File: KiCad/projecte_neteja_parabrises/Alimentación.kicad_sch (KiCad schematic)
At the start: 12 parts, among them U1 LM1117DT-3.3, U2 LM2596S-5

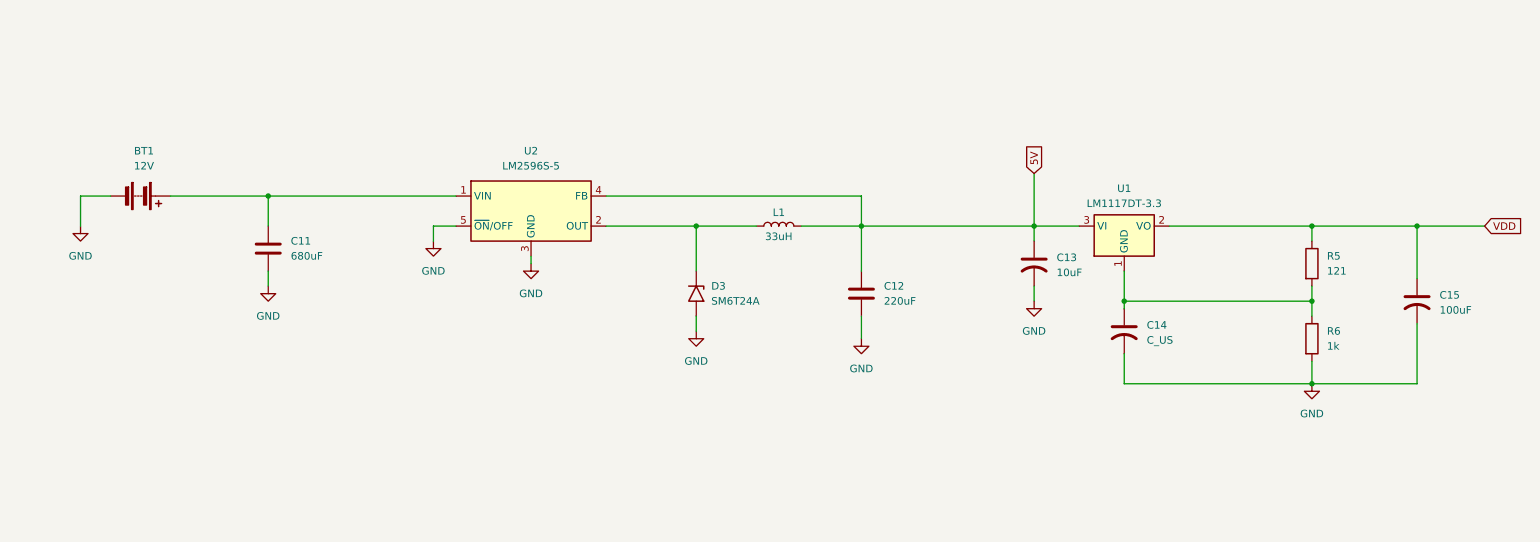
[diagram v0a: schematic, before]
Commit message: millora alimentacio
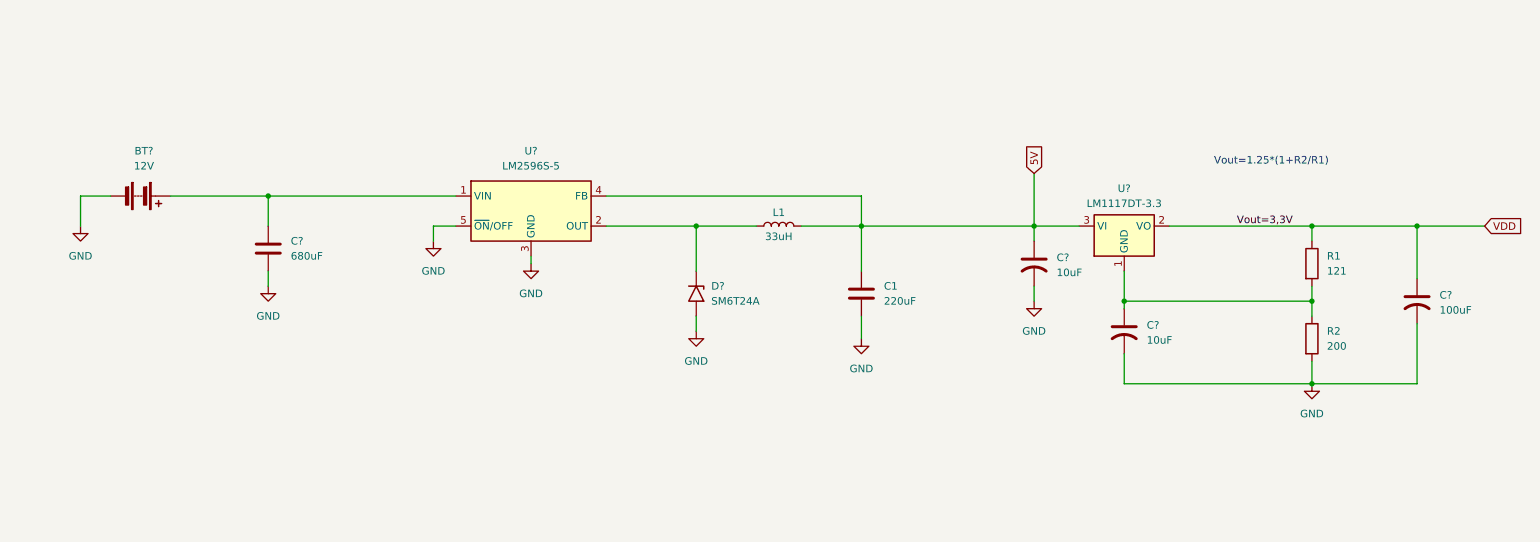
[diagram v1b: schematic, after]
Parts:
- C?: renamed from C14; value C_US -> 10uF
- R2: renamed from R6; value 1k -> 200
- renumbered BT1 to BT?, C12 to C1, C13 to C?, C11 to C?, C15 to C?, D3 to D?, R5 to R1, U1 to U?, U2 to U?
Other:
- note added: "Vout=1.25*(1+R2/R1)"
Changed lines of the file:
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@@
 	(generator_version "9.0")
 	(paper "A4")
+	(text "Vout=1.25*(1+R2/R1)"
+		(exclude_from_sim no)
+		(at 229.362 74.168 0)
+		(effects
+			(font
+				(size 1.27 1.27)
+			)
+		)
+	)
 	(junction
 		(at 254 85.09)
@@
 		)
 	)
+	(label "Vout=3,3V"
+		(at 223.52 85.09 0)
+		(effects
+			(font
+				(size 1.27 1.27)
+			)
+			(justify left bottom)
+		)
+	)
 	(global_label "VDD"
 		(shape input)
@@
 		(dnp no)
 		(fields_autoplaced yes)
-		(property "Reference" "#PWR018"
+		(property "Reference" "#PWR?"
 			(at 236.22 118.11 0)
 			(effects
@@
 		(dnp no)
 		(fields_autoplaced yes)
-		(property "Reference" "U1"
+		(property "Reference" "U?"
 			(at 204.47 78.74 0)
 			(effects
@@
 		(dnp no)
 		(fields_autoplaced yes)
-		(property "Reference" "R6"
+		(property "Reference" "R2"
 			(at 238.76 102.8699 0)
 			(effects
@@
 			)
 		)
-		(property "Value" "1k"
+		(property "Value" "200"
 			(at 238.76 105.4099 0)
 			(effects
@@
 			(project "Alimentación"
 				(path "/2ad4f79a-6f2e-459e-be48-40e5d52d2cdd"
-					(reference "R?")
+					(reference "R2")
 					(unit 1)
 				)
@@
 		(dnp no)
 		(fields_autoplaced yes)
-		(property "Reference" "C13"
+		(property "Reference" "C?"
 			(at 193.04 90.4239 0)
 			(effects
@@
 		(dnp no)
 		(fields_autoplaced yes)
-		(property "Reference" "#PWR0105"
+		(property "Reference" "#PWR02"
 			(at 160.02 110.49 0)
 			(effects
@@
 		(dnp no)
 		(fields_autoplaced yes)
-		(property "Reference" "#PWR0104"
+		(property "Reference" "#PWR01"
 			(at 87.63 93.98 0)
 			(effects
@@
 		(dnp no)
 		(fields_autoplaced yes)
-		(property "Reference" "#PWR017"
+		(property "Reference" "#PWR?"
 			(at 189.23 104.14 0)
 			(effects
@@
 		(dnp no)
 		(fields_autoplaced yes)
-		(property "Reference" "#PWR015"
+		(property "Reference" "#PWR?"
 			(at 59.69 101.6 0)
 			(effects
@@
 		(dnp no)
 		(fields_autoplaced yes)
-		(property "Reference" "#PWR014"
+		(property "Reference" "#PWR?"
 			(at 132.08 109.22 0)
 			(effects
@@
 		(dnp no)
 		(fields_autoplaced yes)
-		(property "Reference" "C12"
+		(property "Reference" "C1"
 			(at 163.83 95.2499 0)
 			(effects
@@
 		(dnp no)
 		(fields_autoplaced yes)
-		(property "Reference" "BT1"
+		(property "Reference" "BT?"
 			(at 38.6715 72.39 90)
 			(effects
@@
 		(dnp no)
 		(fields_autoplaced yes)
-		(property "Reference" "C11"
+		(property "Reference" "C?"
 			(at 63.5 87.6299 0)
 			(effects
@@
 		(dnp no)
 		(fields_autoplaced yes)
-		(property "Reference" "R5"
+		(property "Reference" "R1"
 			(at 238.76 90.1699 0)
 			(effects
@@
 			(project "Alimentación"
 				(path "/2ad4f79a-6f2e-459e-be48-40e5d52d2cdd"
-					(reference "R?")
+					(reference "R1")
 					(unit 1)
 				)
@@
 		(dnp no)
 		(fields_autoplaced yes)
-		(property "Reference" "U2"
+		(property "Reference" "U?"
 			(at 104.14 72.39 0)
 			(effects
@@
 		(dnp no)
 		(fields_autoplaced yes)
-		(property "Reference" "#PWR02"
+		(property "Reference" "#PWR?"
 			(at 104.14 97.79 0)
 			(effects
@@
 		(dnp no)
 		(fields_autoplaced yes)
-		(property "Reference" "#PWR01"
+		(property "Reference" "#PWR?"
 			(at 27.94 91.44 0)
 			(effects
@@
 		(dnp no)
 		(fields_autoplaced yes)
-		(property "Reference" "C15"
+		(property "Reference" "C?"
 			(at 257.81 96.7739 0)
 			(effects
@@
 		(dnp no)
 		(fields_autoplaced yes)
-		(property "Reference" "D3"
+		(property "Reference" "D?"
 			(at 134.62 95.2499 90)
 			(effects
@@
 		(dnp no)
 		(fields_autoplaced yes)
-		(property "Reference" "C14"
+		(property "Reference" "C?"
 			(at 208.28 101.8539 0)
 			(effects
@@
 			)
 		)
-		(property "Value" "C_US"
+		(property "Value" "10uF"
 			(at 208.28 104.3939 0)
 			(effects

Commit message: Actualización huellas
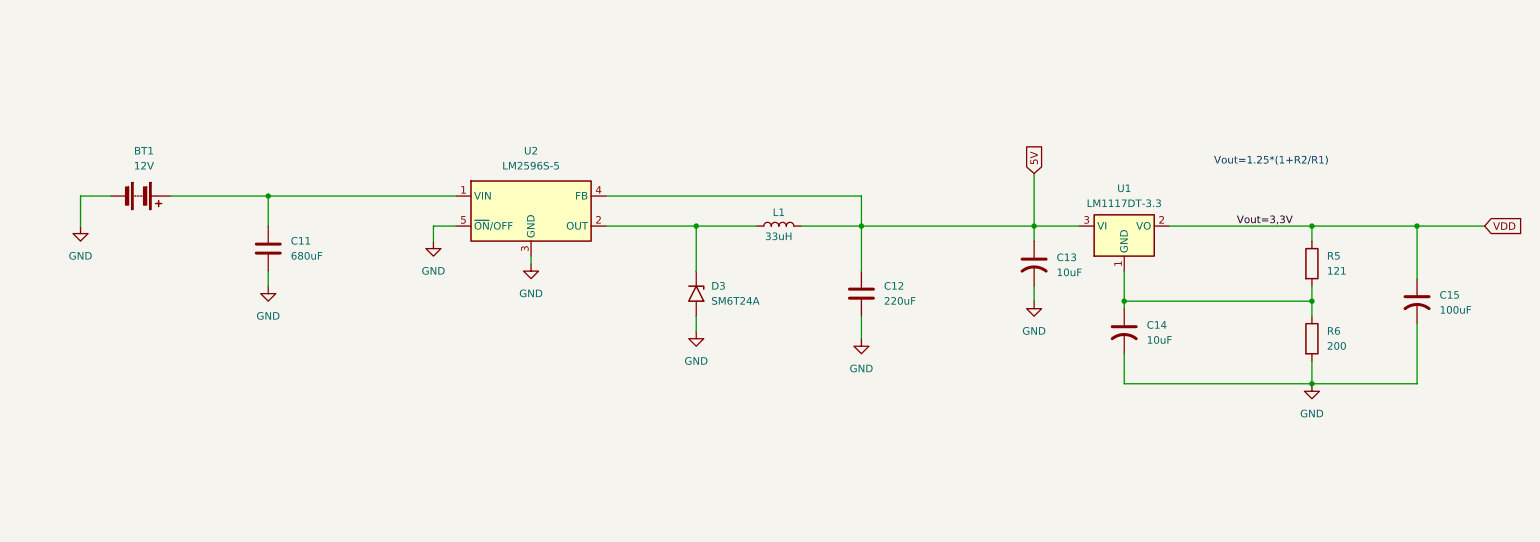
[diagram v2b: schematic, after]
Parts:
- L1: footprint (none) -> Inductor_SMD:L_0603_1608Metric_Pad1.05x0.95mm_HandSolder
- gave numbers to parts that had none: 8
- renumbered C1 to C12, R1 to R5, R2 to R6
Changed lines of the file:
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@@
 		(dnp no)
 		(fields_autoplaced yes)
-		(property "Reference" "#PWR?"
+		(property "Reference" "#PWR018"
 			(at 236.22 118.11 0)
 			(effects
@@
 		(dnp no)
 		(fields_autoplaced yes)
-		(property "Reference" "U?"
+		(property "Reference" "U1"
 			(at 204.47 78.74 0)
 			(effects
@@
 		(dnp no)
 		(fields_autoplaced yes)
-		(property "Reference" "R2"
+		(property "Reference" "R6"
 			(at 238.76 102.8699 0)
 			(effects
@@
 		(dnp no)
 		(fields_autoplaced yes)
-		(property "Reference" "C?"
+		(property "Reference" "C13"
 			(at 193.04 90.4239 0)
 			(effects
@@
 		(dnp no)
 		(fields_autoplaced yes)
-		(property "Reference" "#PWR02"
+		(property "Reference" "#PWR0105"
 			(at 160.02 110.49 0)
 			(effects
@@
 		(dnp no)
 		(fields_autoplaced yes)
-		(property "Reference" "#PWR01"
+		(property "Reference" "#PWR0104"
 			(at 87.63 93.98 0)
 			(effects
@@
 		(dnp no)
 		(fields_autoplaced yes)
-		(property "Reference" "#PWR?"
+		(property "Reference" "#PWR017"
 			(at 189.23 104.14 0)
 			(effects
@@
 		(dnp no)
 		(fields_autoplaced yes)
-		(property "Reference" "#PWR?"
+		(property "Reference" "#PWR015"
 			(at 59.69 101.6 0)
 			(effects
@@
 		(dnp no)
 		(fields_autoplaced yes)
-		(property "Reference" "#PWR?"
+		(property "Reference" "#PWR014"
 			(at 132.08 109.22 0)
 			(effects
@@
 		(dnp no)
 		(fields_autoplaced yes)
-		(property "Reference" "C1"
+		(property "Reference" "C12"
 			(at 163.83 95.2499 0)
 			(effects
@@
 		(dnp no)
 		(fields_autoplaced yes)
-		(property "Reference" "BT?"
+		(property "Reference" "BT1"
 			(at 38.6715 72.39 90)
 			(effects
@@
 		(dnp no)
 		(fields_autoplaced yes)
-		(property "Reference" "C?"
+		(property "Reference" "C11"
 			(at 63.5 87.6299 0)
 			(effects
@@
 		(dnp no)
 		(fields_autoplaced yes)
-		(property "Reference" "R1"
+		(property "Reference" "R5"
 			(at 238.76 90.1699 0)
 			(effects
@@
 		(dnp no)
 		(fields_autoplaced yes)
-		(property "Reference" "U?"
+		(property "Reference" "U2"
 			(at 104.14 72.39 0)
 			(effects
@@
 		(dnp no)
 		(fields_autoplaced yes)
-		(property "Reference" "#PWR?"
+		(property "Reference" "#PWR02"
 			(at 104.14 97.79 0)
 			(effects
@@
 		(dnp no)
 		(fields_autoplaced yes)
-		(property "Reference" "#PWR?"
+		(property "Reference" "#PWR01"
 			(at 27.94 91.44 0)
 			(effects
@@
 		(dnp no)
 		(fields_autoplaced yes)
-		(property "Reference" "C?"
+		(property "Reference" "C15"
 			(at 257.81 96.7739 0)
 			(effects
@@
 			)
 		)
-		(property "Footprint" ""
+		(property "Footprint" "Inductor_SMD:L_0603_1608Metric_Pad1.05x0.95mm_HandSolder"
 			(at 146.05 85.09 0)
 			(effects
@@
 		(dnp no)
 		(fields_autoplaced yes)
-		(property "Reference" "D?"
+		(property "Reference" "D3"
 			(at 134.62 95.2499 90)
 			(effects
@@
 		(dnp no)
 		(fields_autoplaced yes)
-		(property "Reference" "C?"
+		(property "Reference" "C14"
 			(at 208.28 101.8539 0)
 			(effects

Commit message: huella bateria
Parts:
- BT1: footprint (none) -> TerminalBlock:TerminalBlock_MaiXu_MX126-5.0-02P_1x02_P5.00mm
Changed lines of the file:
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@@
 			)
 		)
-		(property "Footprint" ""
+		(property "Footprint" "TerminalBlock:TerminalBlock_MaiXu_MX126-5.0-02P_1x02_P5.00mm"
 			(at 39.624 80.01 90)
 			(effects

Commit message: huella c electrolitica
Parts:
- C13, C14, C15: footprint Capacitor_SMD:C_0805_2012Metric -> Capacitor_THT:CP_Radial_D5.0mm_P2.50mm
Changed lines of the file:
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@@
 			)
 		)
-		(property "Footprint" "Capacitor_SMD:C_0805_2012Metric"
+		(property "Footprint" "Capacitor_THT:CP_Radial_D5.0mm_P2.50mm"
 			(at 189.23 91.44 0)
 			(effects
@@
 			)
 		)
-		(property "Footprint" "Capacitor_SMD:C_0805_2012Metric"
+		(property "Footprint" "Capacitor_THT:CP_Radial_D5.0mm_P2.50mm"
 			(at 254 97.79 0)
 			(effects
@@
 			)
 		)
-		(property "Footprint" "Capacitor_SMD:C_0805_2012Metric"
+		(property "Footprint" "Capacitor_THT:CP_Radial_D5.0mm_P2.50mm"
 			(at 204.47 102.87 0)
 			(effects

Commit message: formula
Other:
- note added: "Vout=1.25*(1+R5/R6)"
- note removed: "Vout=1.25*(1+R2/R1)"
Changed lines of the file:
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@@
 	(generator_version "9.0")
 	(paper "A4")
-	(text "Vout=1.25*(1+R2/R1)"
+	(text "Vout=1.25*(1+R5/R6)"
 		(exclude_from_sim no)
 		(at 229.362 74.168 0)

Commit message: Led
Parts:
- added D2: LED, LED_SMD:LED_0805_2012Metric_Pad1.15x1.40mm_HandSolder, symbol Device:LED
- added R8: 1k, Resistor_SMD:R_0603_1608Metric_Pad0.98x0.95mm_HandSolder, symbol Device:R
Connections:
- net GND: now also R8.1
- new net: D2.1 (K), R8.2
- new net VCC: D2.2 (A)

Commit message: potencia cambios
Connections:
- net VCC is gone; now on net VDD: D2.2 (A)
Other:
- moved on the sheet: D2, R8
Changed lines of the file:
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@@
 	(wire
 		(pts
-			(xy 40.005 128.27) (xy 40.005 130.175)
+			(xy 229.235 55.88) (xy 229.235 57.785)
 		)
 		(stroke
@@
 	(wire
 		(pts
+			(xy 245.11 55.88) (xy 254 55.88)
+		)
+		(stroke
+			(width 0)
+			(type default)
+		)
+	)
+	(wire
+		(pts
 			(xy 236.22 111.76) (xy 254 111.76)
 		)
@@
 	(wire
 		(pts
-			(xy 40.64 128.27) (xy 40.005 128.27)
+			(xy 229.87 55.88) (xy 229.235 55.88)
 		)
 		(stroke
@@
 		(pts
 			(xy 204.47 106.68) (xy 204.47 111.76)
+		)
+		(stroke
+			(width 0)
+			(type default)
+		)
+	)
+	(wire
+		(pts
+			(xy 254 55.88) (xy 254 85.09)
 		)
 		(stroke
@@
 			)
 			(justify left bottom)
-		)
-	)
-	(global_label "VCC"
-		(shape input)
-		(at 55.88 128.27 0)
-		(fields_autoplaced yes)
-		(effects
-			(font
-				(size 1.27 1.27)
-			)
-			(justify left)
-		)
-		(property "Intersheetrefs" "${INTERSHEET_REFS}"
-			(at 62.4938 128.27 0)
-			(effects
-				(font
-					(size 1.27 1.27)
-				)
-				(justify left)
-				(hide yes)
-			)
 		)
 	)
@@
 	(symbol
 		(lib_id "power:GND")
-		(at 40.005 130.175 0)
+		(at 229.235 57.785 0)
 		(unit 1)
 		(exclude_from_sim no)
@@
 		(fields_autoplaced yes)
 		(property "Reference" "#PWR038"
-			(at 40.005 136.525 0)
+			(at 229.235 64.135 0)
 			(effects
 				(font
@@
 		)
 		(property "Value" "GND"
-			(at 40.005 135.255 0)
+			(at 229.235 62.865 0)
 			(effects
 				(font
@@
 		)
 		(property "Footprint" ""
-			(at 40.005 130.175 0)
+			(at 229.235 57.785 0)
 			(effects
 				(font
@@
 		)
 		(property "Datasheet" ""
-			(at 40.005 130.175 0)
+			(at 229.235 57.785 0)
 			(effects
 				(font
@@
 		)
 		(property "Description" "Power symbol creates a global label with name \"GND\" , ground"
-			(at 40.005 130.175 0)
+			(at 229.235 57.785 0)
 			(effects
 				(font
@@
 		)
 		(instances
+			(project "Alimentación"
+				(path "/2ad4f79a-6f2e-459e-be48-40e5d52d2cdd"
+					(reference "#PWR?")
+					(unit 1)
+				)
+			)
 			(project "projecte_neteja_parabrises"
 				(path "/83fe8808-b70b-463e-9fcd-89556c9690a9/a8962c48-b3a9-4541-b459-e1566624b900"
@@
 	(symbol
 		(lib_id "Device:LED")
-		(at 52.07 128.27 0)
+		(at 241.3 55.88 0)
 		(unit 1)
 		(exclude_from_sim no)
@@
 		(fields_autoplaced yes)
 		(property "Reference" "D2"
-			(at 50.4825 122.555 0)
+			(at 239.7125 50.165 0)
 			(effects
 				(font
@@
 		)
 		(property "Value" "LED"
-			(at 50.4825 125.095 0)
+			(at 239.7125 52.705 0)
 			(effects
 				(font
@@
 		)
 		(property "Footprint" "LED_SMD:LED_0805_2012Metric_Pad1.15x1.40mm_HandSolder"
-			(at 52.07 128.27 0)
+			(at 241.3 55.88 0)
 			(effects
 				(font
@@
 		)
 		(property "Datasheet" "~"
-			(at 52.07 128.27 0)
+			(at 241.3 55.88 0)
 			(effects
 				(font
@@
 		)
 		(property "Description" "Light emitting diode"
-			(at 52.07 128.27 0)
+			(at 241.3 55.88 0)
 			(effects
 				(font
@@
 		)
 		(property "Sim.Pins" "1=K 2=A"
-			(at 52.07 128.27 0)
+			(at 241.3 55.88 0)
 			(effects
 				(font
@@
 		)
 		(instances
+			(project "Alimentación"
+				(path "/2ad4f79a-6f2e-459e-be48-40e5d52d2cdd"
+					(reference "D?")
+					(unit 1)
+				)
+			)
 			(project "projecte_neteja_parabrises"
 				(path "/83fe8808-b70b-463e-9fcd-89556c9690a9/a8962c48-b3a9-4541-b459-e1566624b900"
@@
 	(symbol
 		(lib_id "Device:R")
-		(at 44.45 128.27 90)
+		(at 233.68 55.88 90)
 		(unit 1)
 		(exclude_from_sim no)
@@
 		(fields_autoplaced yes)
 		(property "Reference" "R8"
-			(at 44.45 122.555 90)
+			(at 233.68 50.165 90)
 			(effects
 				(font
@@
 		)
 		(property "Value" "1k"
-			(at 44.45 125.095 90)
+			(at 233.68 52.705 90)
 			(effects
 				(font
@@
 		)
 		(property "Footprint" "Resistor_SMD:R_0603_1608Metric_Pad0.98x0.95mm_HandSolder"
-			(at 44.45 130.048 90)
+			(at 233.68 57.658 90)
 			(effects
 				(font
@@
 		)
 		(property "Datasheet" "~"
-			(at 44.45 128.27 0)
+			(at 233.68 55.88 0)
 			(effects
 				(font
@@
 		)
 		(property "Description" "Resistor"
-			(at 44.45 128.27 0)
+			(at 233.68 55.88 0)
 			(effects
 				(font
@@
 		)
 		(instances
+			(project "Alimentación"
+				(path "/2ad4f79a-6f2e-459e-be48-40e5d52d2cdd"
+					(reference "R?")
+					(unit 1)
+				)
+			)
 			(project "projecte_neteja_parabrises"
 				(path "/83fe8808-b70b-463e-9fcd-89556c9690a9/a8962c48-b3a9-4541-b459-e1566624b900"
